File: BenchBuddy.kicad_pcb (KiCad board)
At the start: 4 copper layers, 165.1 x 63.5 mm, 133 parts, among them K1 1461069-5, P1 24 Pin MiniFit JR, P2 CONN_3X2, P3 CONN_2, P4 12 Pin Terminal Block, P5 3 Pin TB, Q1 2N3904, Q2 DMN65D8L-7, Q3 AOD476, Q4 AOD476, SW1 Power Switch, U1 LTV-816S, U11 LM317, U2 MCP3901, U3 LMT84, U4 OPA4170, U5 MCP4801, U6 LM337T, U7 AP5726, U8 LM337T, U9 LM317

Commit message: Layout Work Session 8
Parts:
- removed JP1, JP2, JP3, JP4: JUMPER, PIN_ARRAY_2X1
- removed TP1: CONN_1, 1pin
- added SP1: PWR_STAR_POINT, BenchBudEE:GND_STAR_POINT, F.Cu at (88.3, 113.5)
- C2: footprint SM1206 -> Capacitors_SMD:c_1206
- R2, R5: moved to F.Cu
- moved R43 49.3 mm to (143.2, 98.6), turned to 90 degrees
- moved D4 16.4 mm to (206.4, 103.4)
- moved L1 16.1 mm to (100.2, 113.4)
- moved R1 15.9 mm to (159.5, 137.8), turned to 0 degrees
- moved C12 12.4 mm to (163.8, 109.1)
- moved R2 9.53 mm to (175.0, 127.1), turned to 0 degrees
- moved TH2 8.13 mm to (93.6, 124.3)
- moved R29 7.29 mm to (128.0, 132.8)
- moved R26 6.99 mm to (120.4, 132.8)
- moved R27 6.99 mm to (122.9, 132.8)
- moved R28 6.86 mm to (125.5, 132.8)
- moved R33 6.55 mm to (140.7, 132.8)
- moved R31 6.28 mm to (135.6, 132.8)
- moved R32 6.14 mm to (138.2, 132.8)
- moved R30 5.92 mm to (133.1, 132.8)
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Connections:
- ARD1 pad 10: (no net) -> Net-(ARD1-Pad10)
- ARD1 pad 17: (no net) -> Net-(ARD1-Pad17)
- ARD1 pad 25: (no net) -> Net-(ARD1-Pad25)
- ARD1 pad 26: (no net) -> Net-(ARD1-Pad26)
- ARD1 pad 27: (no net) -> Net-(ARD1-Pad27)
- ARD1 pad 28: (no net) -> Net-(ARD1-Pad28)
- ARD1 pad 9: (no net) -> Net-(ARD1-Pad9)
- P1 pad 1: (no net) -> Net-(P1-Pad1)
- P1 pad 11: (no net) -> Net-(P1-Pad11)
- P1 pad 13: (no net) -> Net-(P1-Pad13)
- P1 pad 15: (no net) -> Net-(P1-Pad15)
- P1 pad 17: (no net) -> Net-(P1-Pad17)
- P1 pad 18: (no net) -> Net-(P1-Pad18)
- P1 pad 19: (no net) -> Net-(P1-Pad19)
- P1 pad 20: (no net) -> Net-(P1-Pad20)
- P1 pad 21: (no net) -> Net-(P1-Pad21)
- P1 pad 22: (no net) -> Net-(P1-Pad22)
- P1 pad 23: (no net) -> Net-(P1-Pad23)
- P1 pad 24: (no net) -> Net-(P1-Pad24)
- P1 pad 7: (no net) -> Net-(P1-Pad7)
- P1 pad 8: (no net) -> Net-(P1-Pad8)
- P1 pad 9: (no net) -> Net-(P1-Pad9)
- U2 pad 10: (no net) -> REF-
- U2 pad 15: (no net) -> Net-(U2-Pad15)
- U2 pad 16: (no net) -> Net-(U2-Pad16)
- U2 pad 9: (no net) -> REF+
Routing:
- net +12C: track 187.2 -> 56.8 mm, vias 2 -> 1
- net /Arduino/RELAY+: track 0.00 -> 52.9 mm
- net /Arduino/RELAY-: track 0.00 -> 44.7 mm
- net Net-(D2-Pad1): track 0.00 -> 21.2 mm
- net GND: track 32.1 -> 11.0 mm
- net Net-(D2-Pad2): track 0.00 -> 20.4 mm
- net +12P: track 48.7 -> 63.1 mm, vias 2 -> 3
- net Net-(D1-Pad1): track 0.00 -> 11.1 mm, vias 0 -> 1
- net Net-(Q1-Pad1): track 0.00 -> 10.3 mm
- net Net-(R3-Pad2): track 0.00 -> 6.99 mm
- net Net-(R1-Pad2): track 0.00 -> 5.18 mm, vias 0 -> 1
- net Net-(P1-Pad4): track 50.3 -> 55.3 mm
- net Net-(Q1-Pad2): track 0.00 -> 4.31 mm
- net Net-(ARD1-Pad8): track 0.00 -> 4.09 mm
- net Net-(ARD1-Pad3): track 0.00 -> 4.09 mm
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
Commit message: Layout Work Session 9
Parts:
- moved C22 9.45 mm to (175.9, 90.3), turned to 270 degrees
- moved C17 7.58 mm to (178.5, 90.3), turned to 270 degrees
- moved D10 7.15 mm to (195.7, 90.4)
- moved R52 6.52 mm to (198.1, 80.9)
- moved C16 5.99 mm to (155.3, 90.5), turned to 270 degrees
- moved D8 5.44 mm to (174.4, 83.0), turned to 270 degrees
- moved C19 2.22 mm to (173.4, 90.3), turned to 270 degrees
- moved C20 1.94 mm to (196.7, 86.6)
- moved C21 1.60 mm to (199.8, 85.8), turned to 180 degrees
- moved D9 1.56 mm to (186.2, 85.7)
- moved R21 1.54 mm to (140.6, 79.3)
- moved C23 1.40 mm to (157.9, 90.5), turned to 270 degrees
- moved C18 1.40 mm to (160.4, 90.5), turned to 270 degrees
- moved D3 1.17 mm to (155.2, 83.2)
- moved R54 0.88 mm to (191.8, 85.4)
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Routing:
- net /PowerAdjustmentMonitor/V-_ADJ: track 0.00 -> 90.7 mm
- net /PowerAdjustmentMonitor/V+_ADJ: track 0.00 -> 90.2 mm
- net Net-(C18-Pad1): track 0.00 -> 59.0 mm
- net Net-(C19-Pad1): track 0.00 -> 50.1 mm
- net GND_PWR: track 0.00 -> 23.7 mm, vias 0 -> 1
- net +12V: track 212.7 -> 218.1 mm
- net +3.3V: track 145.5 -> 149.8 mm, vias 0 -> 1
- net -12V: track 215.9 -> 216.9 mm

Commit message: Layout Work Session 10
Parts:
- C2, C6: moved to F.Cu
- moved C6 38.7 mm to (208.3, 119.6), turned to 0 degrees
- moved L1 16.7 mm to (83.6, 115.3)
- moved C5 11.8 mm to (155.3, 120.1)
- moved R17 10.7 mm to (162.6, 115.7), turned to 180 degrees
- moved U7 9.08 mm to (160.8, 118.4), turned to 90 degrees
- moved TH2 7.51 mm to (86.1, 124.8)
- moved R23 7.43 mm to (149.4, 101.7)
- moved C2 6.91 mm to (83.6, 106.5), turned to 270 degrees
- moved D5 6.83 mm to (172.2, 120.1), turned to 270 degrees
- moved L4 6.76 mm to (167.6, 120.9), turned to 90 degrees
- moved R24 6.70 mm to (147.1, 99.5)
- moved TH4 5.64 mm to (76.5, 115.6)
- moved C12 5.03 mm to (158.8, 109.0)
- moved R22 4.32 mm to (151.8, 98.4)
- moved R25 4.21 mm to (149.3, 98.4)
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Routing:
- net +5P: track 9.94 -> 209.5 mm, vias 3 -> 2
- net +12C: track 56.8 -> 182.6 mm, vias 1 -> 2
- net /LED_Driver/LED_STRING+: track 0.00 -> 66.0 mm, vias 0 -> 2
- net /LED_Driver/LED_STRING-: track 0.00 -> 58.6 mm, vias 0 -> 2
- net Net-(D5-Pad1): track 0.00 -> 13.3 mm
- net Net-(P1-Pad14): track 19.8 -> 14.0 mm
- net Net-(P1-Pad4): track 55.3 -> 50.2 mm
- net -12P: track 30.2 -> 35.2 mm
- net GND_LED: track 2.83 -> 7.22 mm, vias 1 -> 4
- net GND: track 11.0 -> 7.09 mm, vias 0 -> 1
- net +5V: track 7.38 -> 7.97 mm, vias 3 -> 2

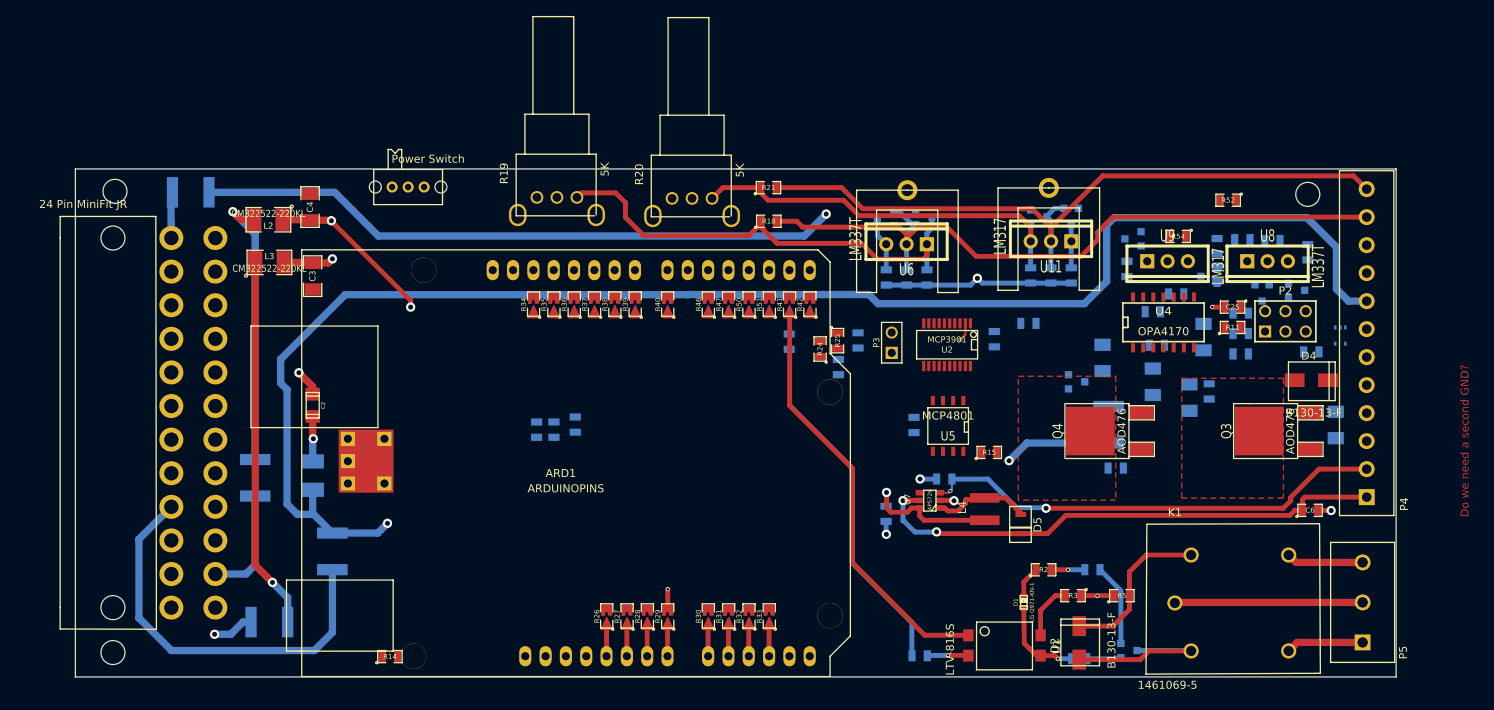
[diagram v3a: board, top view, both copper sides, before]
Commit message: Layout Work Session 12
Pulled from CE.

Session 11 missed due to corrupted pcb file pulled from CE
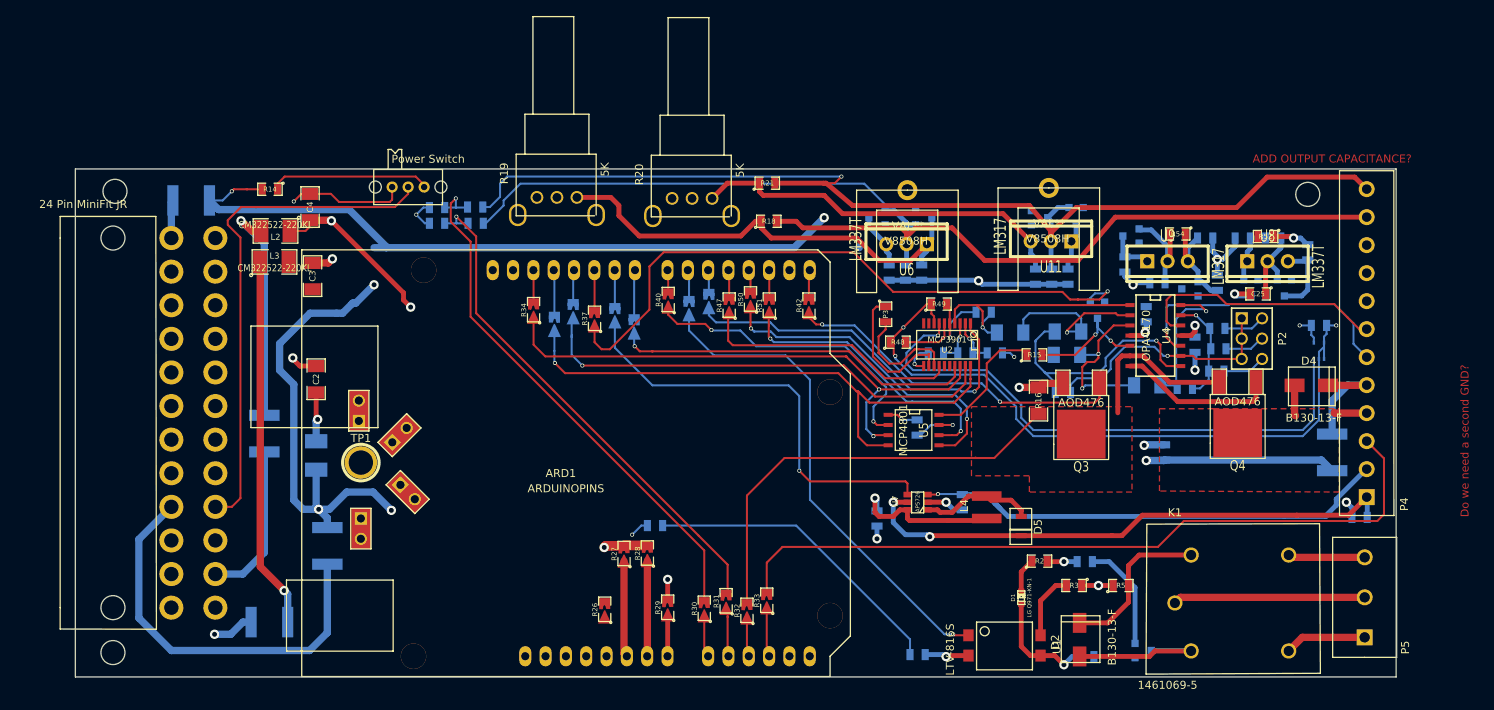
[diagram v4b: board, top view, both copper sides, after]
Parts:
- removed SP1: PWR_STAR_POINT, BenchBudEE:GND_STAR_POINT
- added JP1: JUMPER, GND_POINT, F.Cu at (94.5, 110.2)
- added JP2: JUMPER, GND_POINT, F.Cu at (89.4, 107.2)
- added JP3: JUMPER, GND_POINT, F.Cu at (95.5, 117.3)
- added JP4: JUMPER, GND_POINT, F.Cu at (89.7, 121.9)
- added L5: INDUCTOR, SM0805, B.Cu at (165.2, 99.9)
- added TP1: CONN_1, 1pin, F.Cu at (89.7, 113.7)
- C2: footprint Capacitors_SMD:c_1206 -> SM1206
- C6, R11, R24, R25, R35, R36, R38, R39, R41, R46: moved to B.Cu
- P3: footprint PIN_ARRAY_2X1 -> SM0805
- R16, R48, R49: moved to F.Cu
- moved R14 60.3 mm to (78.3, 79.5), turned to 180 degrees
- moved C7 58.1 mm to (168.9, 99.9), turned to 180 degrees
- moved R23 54.0 mm to (99.2, 81.8), turned to 0 degrees
- moved C1 53.0 mm to (167.5, 94.9), turned to 180 degrees
- moved R22 50.7 mm to (103.9, 81.7), turned to 0 degrees
- moved R24 50.4 mm to (99.2, 83.8), turned to 180 degrees
- moved C8 48.7 mm to (161.5, 99.9), turned to 180 degrees
- moved R25 47.6 mm to (104.0, 83.8), turned to 180 degrees
- moved R16 37.3 mm to (174.4, 105.9)
- moved Q3 29.2 mm to (179.7, 103.8), turned to 180 degrees
- moved R43 28.5 mm to (126.4, 121.5), turned to 180 degrees
- moved TH5 28.2 mm to (211.1, 112.4)
- moved R11 22.7 mm to (177.4, 104.9)
- moved R8 18.9 mm to (170.8, 97.4), turned to 0 degrees
- moved R9 17.0 mm to (178.1, 97.3), turned to 180 degrees
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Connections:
- C7 pad 2: +5V -> Net-(C7-Pad2)
- P4 pad 6: /Thermocouple/TC IN - -> /Thermocouple/TC IN +
- P4 pad 7: /Thermocouple/TC IN + -> /Thermocouple/TC IN -
- R41 pad 2: Net-(ARD1-Pad12) -> Net-(ARD1-Pad17)
- U2 pad 2: +5V -> Net-(C7-Pad2)
- U4 pad 4: FE_V- -> FE_V+
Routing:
- net AGND: track 1.59 -> 130.2 mm, vias 1 -> 13
- net /Fan/TACH_IN: track 0.00 -> 93.5 mm
- net GND: track 7.09 -> 100.3 mm, vias 1 -> 4
- net /Arduino/FAN_PWM: track 0.00 -> 80.7 mm, vias 0 -> 1
- net /Arduino/CURR_MEAS: track 0.00 -> 75.5 mm
- net /Arduino/MOSI: track 0.00 -> 71.7 mm, vias 0 -> 1
- net /Thermocouple/CH1+: track 0.00 -> 71.2 mm, vias 0 -> 1
- net /Arduino/SCLK: track 0.00 -> 70.0 mm, vias 0 -> 2
- net /Arduino/V+_ADJ_MON: track 0.00 -> 67.7 mm, vias 0 -> 1
- net /Arduino/V-_ADJ_MON: track 0.00 -> 64.9 mm, vias 0 -> 1
- net Net-(P1-Pad16): track 0.00 -> 64.0 mm
- net /Arduino/MISO: track 0.00 -> 59.2 mm, vias 0 -> 1
- net /Arduino/LED_EN_PWM: track 0.00 -> 53.7 mm, vias 0 -> 1
- net /PowerAdjustmentMonitor/V-_ADJ: track 90.7 -> 144.2 mm
- net /PowerAdjustmentMonitor/V+_ADJ: track 90.2 -> 142.1 mm, vias 0 -> 1
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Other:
- board text added: "ADD OUTPUT CAPACITANCE?"

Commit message: Layout Work Session 14
Pulled from CE
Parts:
- removed R26: R, SM0805-blob
- added C26: C, SM1210, B.Cu at (212.4, 92.2)
- added C27: C, SM1210, B.Cu at (211.5, 87.3)
- added C28: C, SM1210, B.Cu at (211.6, 83.8)
- added C29: C, SM1210, B.Cu at (211.7, 79.8)
- added C30: C, SM0805, B.Cu at (162.9, 104.4)
- added C31: C, SM0805, F.Cu at (158.2, 94.2)
- added R56: R, SM0805, F.Cu at (210.0, 91.5)
- R27, R28, R29, R30, R31, R32, R33, R34, R35, R36, R37, R38, R39, R40, R41, R42, R46, R47, R50, R51: footprint SM0805-blob -> SM0805-SB
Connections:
- ARD1 pad 10: Net-(ARD1-Pad10) -> (no net)
- ARD1 pad 12: Net-(ARD1-Pad12) -> (no net)
- ARD1 pad 25: Net-(ARD1-Pad25) -> (no net)
- ARD1 pad 26: Net-(ARD1-Pad26) -> (no net)
- ARD1 pad 27: Net-(ARD1-Pad27) -> (no net)
- ARD1 pad 28: Net-(ARD1-Pad28) -> (no net)
- ARD1 pad 9: Net-(ARD1-Pad9) -> (no net)
- P1 pad 1: Net-(P1-Pad1) -> (no net)
- P1 pad 11: Net-(P1-Pad11) -> (no net)
- P1 pad 13: Net-(P1-Pad13) -> (no net)
- P1 pad 15: Net-(P1-Pad15) -> (no net)
- P1 pad 17: Net-(P1-Pad17) -> (no net)
- P1 pad 18: Net-(P1-Pad18) -> (no net)
- P1 pad 19: Net-(P1-Pad19) -> (no net)
- P1 pad 20: Net-(P1-Pad20) -> (no net)
- P1 pad 21: Net-(P1-Pad21) -> (no net)
- P1 pad 22: Net-(P1-Pad22) -> (no net)
- P1 pad 23: Net-(P1-Pad23) -> (no net)
- P1 pad 24: Net-(P1-Pad24) -> (no net)
- P1 pad 7: Net-(P1-Pad7) -> (no net)
- P1 pad 8: Net-(P1-Pad8) -> (no net)
- P1 pad 9: Net-(P1-Pad9) -> (no net)
- U2 pad 10: REF- -> AGND
- U2 pad 9: REF+ -> N-0000070
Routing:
- net N-0000095: track 4.78 -> 51.2 mm
- net /Fan/TACH_IN: track 93.5 -> 117.8 mm
- net AGND: track 130.2 -> 150.8 mm
- net GND_PWR: track 26.7 -> 47.2 mm
- net N-0000099: track 50.3 -> 66.8 mm
- net +5V: track 19.5 -> 32.9 mm
- net N-0000087: track 0.00 -> 5.20 mm
- net /PowerAdjustmentMonitor/V+_ADJ: track 142.1 -> 146.3 mm
- net +5P: track 212.7 -> 216.6 mm
- net N-0000074: track 32.3 -> 28.3 mm
- net N-00000124: track 7.45 -> 11.1 mm
- net N-0000065: track 0.00 -> 3.27 mm, vias 0 -> 1
- net N-0000070: track 0.00 -> 3.21 mm
- net N-0000064: track 0.00 -> 3.12 mm, vias 0 -> 1
- net +12V: track 220.8 -> 223.9 mm
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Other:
- net class Default: clearance 0.254 -> 0.1524
- rule pad_to_mask_clearance: 0.254 -> 0
- rule trace_clearance: 0.254 -> 0.1524
- board text removed: "ADD OUTPUT CAPACITANCE?"
- board text removed: "Do we need a second GND?"
